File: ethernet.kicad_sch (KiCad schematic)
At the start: 1 part, among them U1 MIMX8MN5DVPIZAA

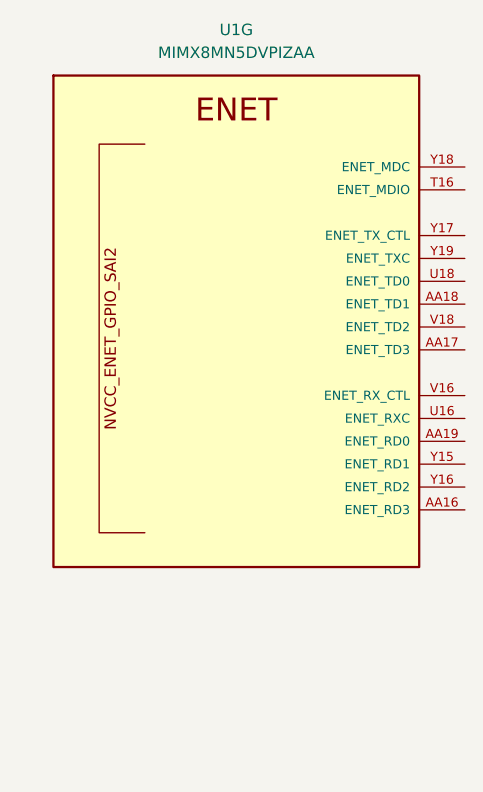
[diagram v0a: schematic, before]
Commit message: move to i.MX8M Mini
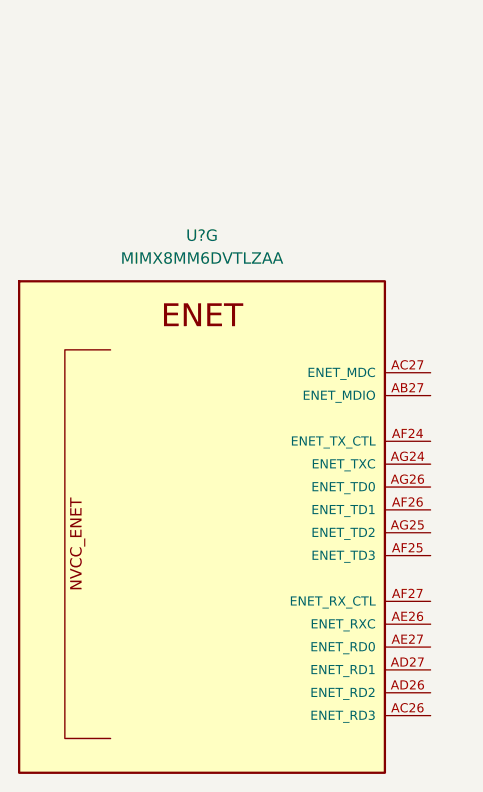
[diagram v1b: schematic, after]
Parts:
- removed U1: MIMX8MN5DVPIZAA, qsbc:SOT1967-1, symbol qsbc:MIMX8MN5DVPIZAA
- added U?: MIMX8MM6DVTLZAA, qsbc:SOT1967-1, symbol qsbc:MIMX8MM6DVTLZAA

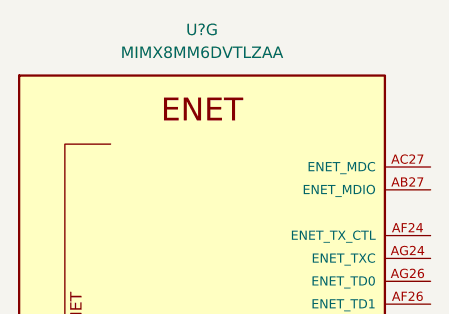
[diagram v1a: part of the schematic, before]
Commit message: ddr sch done
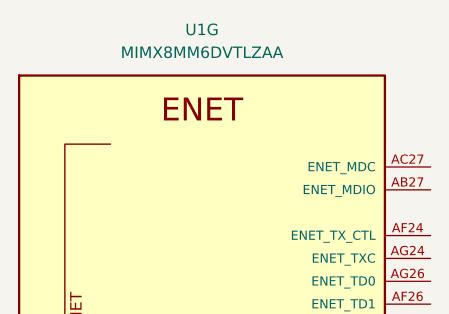
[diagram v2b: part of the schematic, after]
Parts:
- gave numbers to parts that had none: 1
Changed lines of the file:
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@@
   (symbol (lib_id "qsbc:MIMX8MM6DVTLZAA") (at 114.3 90.17 0) (unit 7)
     (in_bom yes) (on_board yes) (fields_autoplaced)
-    (property "Reference" "U?" (id 0) (at 114.3 71.12 0))
+    (property "Reference" "U1" (id 0) (at 114.3 71.12 0))
     (property "Value" "MIMX8MM6DVTLZAA" (id 1) (at 114.3 73.66 0))
     (property "Footprint" "qsbc:SOT1967-1" (id 2) (at 118.11 280.67 0)

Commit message: misc work, usb sch done
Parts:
- added J4: ARJM11D7-502-AB-EW2, qsbc:ARJM11D7-502-AB-EW2, symbol qsbc:ARJM11D7-502-AB-EW2
- added U13, U14: TPD4EUSB30, Package_SON:USON-10_2.5x1.0mm_P0.5mm, symbol qsbc:TPD4EUSB30
- added U18: RTL8211F, Package_DFN_QFN:QFN-40-1EP_5x5mm_P0.4mm_EP3.6x3.6mm_ThermalVias, symbol qsbc:RTL8211F
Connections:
- new net: U14.1 (D1+), U14.10
- new net: U14.2 (D1-), U14.9
- new net: U14.3 (GND), U14.8 (GND)
- new net: U14.4 (D2+), U14.7
- new net: U14.5 (D2-), U14.6
- new net: U13.1 (D1+), U13.10
- new net: U13.2 (D1-), U13.9
- new net: U13.3 (GND), U13.8 (GND)
- new net: U13.4 (D2+), U13.7
- new net: U13.5 (D2-), U13.6
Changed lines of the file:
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@@
 (kicad_sch (version 20211123) (generator eeschema)
-  (paper "A4")
+  (paper "A3")
+  (symbol (lib_id "qsbc:TPD4EUSB30") (at 275.59 53.34 0) (unit 1)
+    (in_bom yes) (on_board yes) (fields_autoplaced)
+    (property "Reference" "U14" (id 0) (at 275.59 40.64 0))
+    (property "Value" "TPD4EUSB30" (id 1) (at 275.59 43.18 0))
+    (property "Footprint" "Package_SON:USON-10_2.5x1.0mm_P0.5mm" (id 2) (at 251.46 63.5 0)
+      (effects (font (size 1.27 1.27)) hide)
+    )
+    (property "Datasheet" "http://www.ti.com/lit/ds/symlink/tpd2eusb30a.pdf" (id 3) (at 275.59 53.34 0)
+      (effects (font (size 1.27 1.27)) hide)
+    )
+    (pin "1")
+    (pin "10")
+    (pin "2")
+    (pin "3")
+    (pin "4")
+    (pin "5")
+    (pin "6")
+    (pin "7")
+    (pin "8")
+    (pin "9")
+  )
+  (symbol (lib_id "qsbc:ARJM11D7-502-AB-EW2") (at 318.77 130.81 0) (unit 1)
+    (in_bom yes) (on_board yes) (fields_autoplaced)
+    (property "Reference" "J4" (id 0) (at 350.52 92.7099 0)
+      (effects (font (size 1.27 1.27)) (justify left))
+    )
+    (property "Value" "ARJM11D7-502-AB-EW2" (id 1) (at 350.52 95.2499 0)
+      (effects (font (size 1.27 1.27)) (justify left))
+    )
+    (property "Footprint" "qsbc:ARJM11D7-502-AB-EW2" (id 2) (at 336.55 140.97 0)
+      (effects (font (size 1.27 1.27)) hide)
+    )
+    (property "Datasheet" "https://abracon.com/Magnetics/ARJM11.pdf" (id 3) (at 340.36 138.43 0)
+      (effects (font (size 1.27 1.27)) hide)
+    )
+    (pin "1")
+    (pin "10")
+    (pin "11")
+    (pin "12")
+    (pin "13")
+    (pin "14")
+    (pin "15")
+    (pin "16")
+    (pin "2")
+    (pin "3")
+    (pin "4")
+    (pin "5")
+    (pin "6")
+    (pin "7")
+    (pin "8")
+    (pin "9")
+  )
   (symbol (lib_id "qsbc:MIMX8MM6DVTLZAA") (at 114.3 90.17 0) (unit 7)
     (in_bom yes) (on_board yes) (fields_autoplaced)
@@
     (pin "D19")
   )
+  (symbol (lib_id "qsbc:TPD4EUSB30") (at 273.05 96.52 0) (unit 1)
+    (in_bom yes) (on_board yes) (fields_autoplaced)
+    (property "Reference" "U13" (id 0) (at 273.05 83.82 0))
+    (property "Value" "TPD4EUSB30" (id 1) (at 273.05 86.36 0))
+    (property "Footprint" "Package_SON:USON-10_2.5x1.0mm_P0.5mm" (id 2) (at 248.92 106.68 0)
+      (effects (font (size 1.27 1.27)) hide)
+    )
+    (property "Datasheet" "http://www.ti.com/lit/ds/symlink/tpd2eusb30a.pdf" (id 3) (at 273.05 96.52 0)
+      (effects (font (size 1.27 1.27)) hide)
+    )
+    (pin "1")
+    (pin "10")
+    (pin "2")
+    (pin "3")
+    (pin "4")
+    (pin "5")
+    (pin "6")
+    (pin "7")
+    (pin "8")
+    (pin "9")
+  )
+  (symbol (lib_id "qsbc:RTL8211F") (at 217.17 158.75 0) (unit 1)
+    (in_bom yes) (on_board yes) (fields_autoplaced)
+    (property "Reference" "U18" (id 0) (at 217.17 148.59 0))
+    (property "Value" "RTL8211F" (id 1) (at 217.17 151.13 0))
+    (property "Footprint" "Package_DFN_QFN:QFN-40-1EP_5x5mm_P0.4mm_EP3.6x3.6mm_ThermalVias" (id 2) (at 260.35 241.3 0)
+      (effects (font (size 1.27 1.27)) hide)
+    )
+    (property "Datasheet" "https://datasheet.lcsc.com/lcsc/1912111437_Realtek-Semicon-RTL8211F-CG_C187932.pdf" (id 3) (at 267.97 245.11 0)
+      (effects (font (size 1.27 1.27)) hide)
+    )
+    (pin "11")
+    (pin "12")
+    (pin "13")
+    (pin "14")
+    (pin "15")
+    (pin "16")
+    (pin "17")
+    (pin "18")
+    (pin "19")
+    (pin "20")
+    (pin "21")
+    (pin "22")
+    (pin "23")
+    (pin "24")
+    (pin "25")
+    (pin "26")
+    (pin "27")
+    (pin "28")
+    (pin "29")
+    (pin "3")
+    (pin "30")
+    (pin "31")
+    (pin "32")
+    (pin "33")
+    (pin "34")
+    (pin "35")
+    (pin "36")
+    (pin "37")
+    (pin "38")
+    (pin "39")
+    (pin "40")
+    (pin "41")
+    (pin "8")
+    (pin "1")
+    (pin "10")
+    (pin "2")
+    (pin "4")
+    (pin "5")
+    (pin "6")
+    (pin "7")
+    (pin "9")
+  )
 )

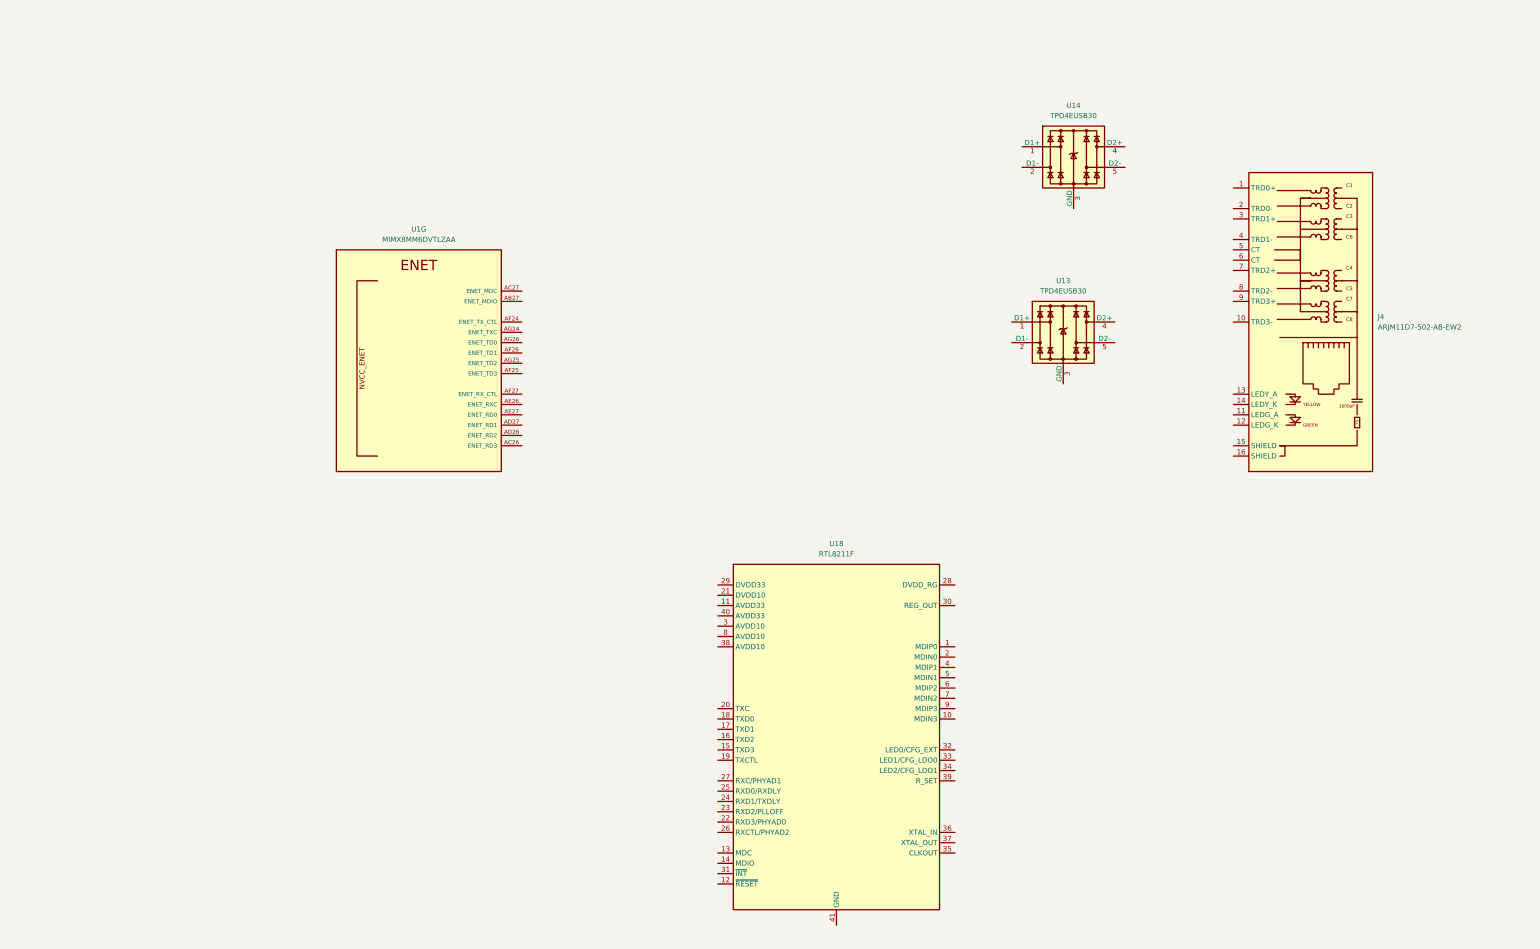
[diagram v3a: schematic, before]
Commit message: enet sch done, other misc sch work
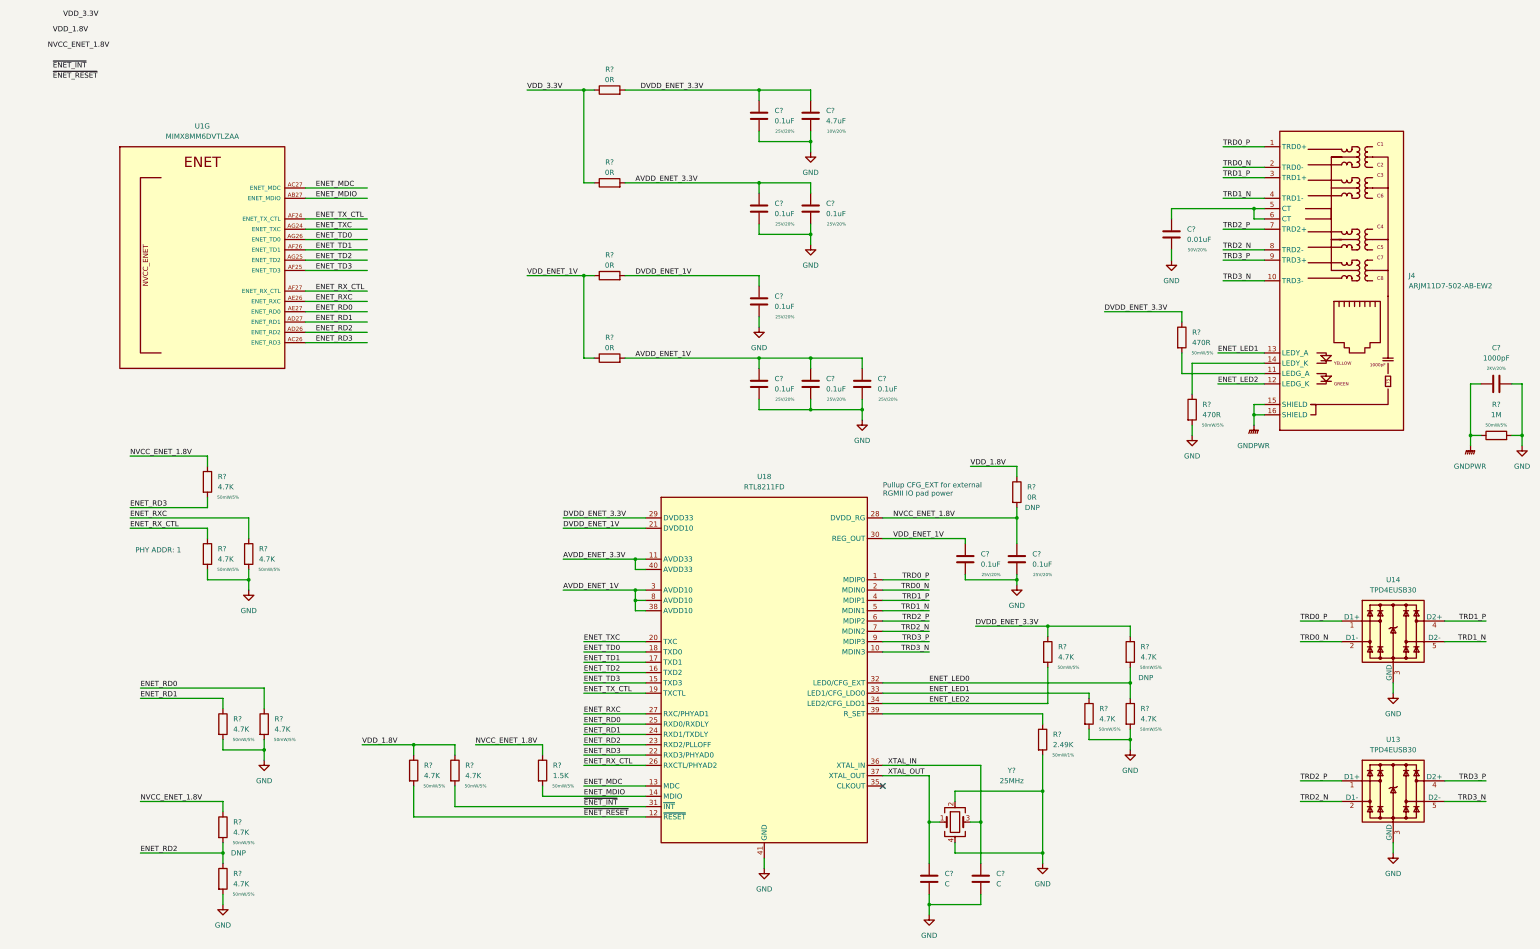
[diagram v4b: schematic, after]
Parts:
- added C? (x9): 0.1uF, Capacitor_SMD:C_0402_1005Metric, symbol Device:C
- added C?: 4.7uF, Capacitor_SMD:C_0402_1005Metric, symbol Device:C
- added C?: 1000pF, Capacitor_SMD:C_1210_3225Metric, symbol Device:C
- added C?: 0.01uF, Capacitor_SMD:C_0603_1608Metric, symbol Device:C
- added C? (x2): C, Capacitor_SMD:C_0402_1005Metric, symbol Device:C
- added R? (x13): 4.7K, Resistor_SMD:R_0402_1005Metric, symbol Device:R
- added R? (x5): 0R, Resistor_SMD:R_0402_1005Metric, symbol Device:R
- added R?: 2.49K, Resistor_SMD:R_0402_1005Metric, symbol Device:R
- added R? (x2): 470R, Resistor_SMD:R_0402_1005Metric, symbol Device:R
- added R?: 1M, Resistor_SMD:R_1206_3216Metric, symbol Device:R
- added R?: 1.5K, Resistor_SMD:R_0402_1005Metric, symbol Device:R
- added Y?: 25MHz, symbol Device:Crystal_GND24
- U18: value RTL8211F -> RTL8211FD
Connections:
- net TRD0_P: now reaches U14.1 (D1+), U14.10
- net TRD0_P: now also J4.1 (TRD0+), U18.1 (MDIP0)
- net TRD0_N: now reaches U14.2 (D1-), U14.9
- net TRD0_N: now also J4.2 (TRD0-), U18.2 (MDIN0)
- net GND: now reaches U14.3 (GND), U14.8 (GND)
- net GND: now also U13.3 (GND), U13.8 (GND), U18.41 (GND), C?.2, C?.2, C?.2, C?.2, C?.2, C?.2, C?.2, C?.2, C?.2, C?.2, C?.2, C?.2, C?.2, C?.2, R?.2, R?.2, R?.2, R?.2, R?.2, R?.2, R?.2, R?.2, R?.2, R?.2, Y?.2, Y?.4
- net TRD1_P: now reaches U14.4 (D2+), U14.7
- net TRD1_P: now also J4.3 (TRD1+), U18.4 (MDIP1)
- net TRD1_N: now reaches U14.5 (D2-), U14.6
- net TRD1_N: now also J4.4 (TRD1-), U18.5 (MDIN1)
- net TRD3_N: now reaches J4.10 (TRD3-)
- net TRD3_N: now also U13.5 (D2-), U13.6, U18.10 (MDIN3)
- net at J4.11 (LEDG_A): now also R?.2
- net ENET_LED2: now reaches J4.12 (LEDG_K)
- net ENET_LED2: now also U18.34 (LED2/CFG_LDO1), R?.2
- net ENET_LED1: now reaches J4.13 (LEDY_A)
- net ENET_LED1: now also U18.33 (LED1/CFG_LDO0), R?.1
- net at J4.14 (LEDY_K): now also R?.1
- net GNDPWR: now reaches J4.15 (SHIELD)
- net GNDPWR: now also J4.16 (SHIELD), C?.1, R?.1
- net at J4.5 (CT): now also J4.6 (CT), C?.1
- net TRD2_P: now reaches J4.7 (TRD2+)
- net TRD2_P: now also U13.1 (D1+), U13.10, U18.6 (MDIP2)
- net TRD2_N: now reaches J4.8 (TRD2-)
- net TRD2_N: now also U13.2 (D1-), U13.9, U18.7 (MDIN2)
- net TRD3_P: now reaches J4.9 (TRD3+)
- net TRD3_P: now also U13.4 (D2+), U13.7, U18.9 (MDIP3)
- net ENET_MDIO: now reaches U1.AB27 (ENET_MDIO)
- net ENET_MDIO: now also U18.14 (MDIO), R?.2
- net ENET_RD3: now reaches U1.AC26 (ENET_RD3)
- net ENET_RD3: now also U18.22 (RXD3/PHYAD0), R?.2
- net ENET_MDC: now reaches U1.AC27 (ENET_MDC)
- net ENET_MDC: now also U18.13 (MDC)
- net ENET_RD2: now reaches U1.AD26 (ENET_RD2)
- net ENET_RD2: now also U18.23 (RXD2/PLLOFF), R?.1, R?.2
- net ENET_RD1: now reaches U1.AD27 (ENET_RD1)
- net ENET_RD1: now also U18.24 (RXD1/TXDLY), R?.1
- net ENET_RXC: now reaches U1.AE26 (ENET_RXC)
- net ENET_RXC: now also U18.27 (RXC/PHYAD1), R?.1
- net ENET_RD0: now reaches U1.AE27 (ENET_RD0)
- net ENET_RD0: now also U18.25 (RXD0/RXDLY), R?.1
- net ENET_TX_CTL: now reaches U1.AF24 (ENET_TX_CTL)
- net ENET_TX_CTL: now also U18.19 (TXCTL)
- net ENET_TD3: now reaches U1.AF25 (ENET_TD3)
- net ENET_TD3: now also U18.15 (TXD3)
- net ENET_TD1: now reaches U1.AF26 (ENET_TD1)
- net ENET_TD1: now also U18.17 (TXD1)
- net ENET_RX_CTL: now reaches U1.AF27 (ENET_RX_CTL)
- net ENET_RX_CTL: now also U18.26 (RXCTL/PHYAD2), R?.1
- net ENET_TXC: now reaches U1.AG24 (ENET_TXC)
- net ENET_TXC: now also U18.20 (TXC)
- net ENET_TD2: now reaches U1.AG25 (ENET_TD2)
- net ENET_TD2: now also U18.16 (TXD2)
- net ENET_TD0: now reaches U1.AG26 (ENET_TD0)
- net ENET_TD0: now also U18.18 (TXD0)
- net AVDD_ENET_3.3V: now reaches U18.11 (AVDD33)
- net AVDD_ENET_3.3V: now also U18.40 (AVDD33), C?.1, C?.1, R?.2
- net ~{ENET_RESET}: now reaches U18.12 (~{RESET})
- net ~{ENET_RESET}: now also R?.2
- net DVDD_ENET_1V: now reaches U18.21 (DVDD10)
- net DVDD_ENET_1V: now also C?.1, R?.2
- net NVCC_ENET_1.8V: now reaches U18.28 (DVDD_RG)
- net NVCC_ENET_1.8V: now also C?.1, R?.1, R?.1, R?.1, R?.2
- net DVDD_ENET_3.3V: now reaches U18.29 (DVDD33)
- net DVDD_ENET_3.3V: now also C?.1, C?.1, R?.1, R?.1, R?.1, R?.2
- net AVDD_ENET_1V: now reaches U18.3 (AVDD10)
- net AVDD_ENET_1V: now also U18.38 (AVDD10), U18.8 (AVDD10), C?.1, C?.1, C?.1, R?.2
- net VDD_ENET_1V: now reaches U18.30 (REG_OUT)
- net VDD_ENET_1V: now also C?.1, R?.1, R?.1
- net ~{ENET_INT}: now reaches U18.31 (~{INT})
- net ~{ENET_INT}: now also R?.2
- net ENET_LED0: now reaches U18.32 (LED0/CFG_EXT)
- net ENET_LED0: now also R?.1, R?.2
- net XTAL_IN: now reaches U18.36 (XTAL_IN)
- net XTAL_IN: now also C?.1, Y?.3
- net XTAL_OUT: now reaches U18.37 (XTAL_OUT)
- net XTAL_OUT: now also C?.1, Y?.1
- net at U18.39 (R_SET): now also R?.1
- new net VDD_1.8V: R?.1, R?.1, R?.1
- new net VDD_3.3V: R?.1, R?.1
- no-connect marks 0 -> 1
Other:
- note added: "PHY ADDR: 1"
- note added: "Pullup CFG_EXT for external RGMII IO pad power"
- moved on the sheet: J4, U13, U14, U18, U1G

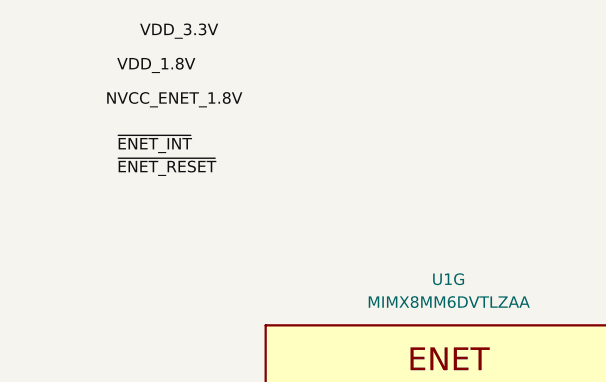
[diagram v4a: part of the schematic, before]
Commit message: enet: add hierarchial labels
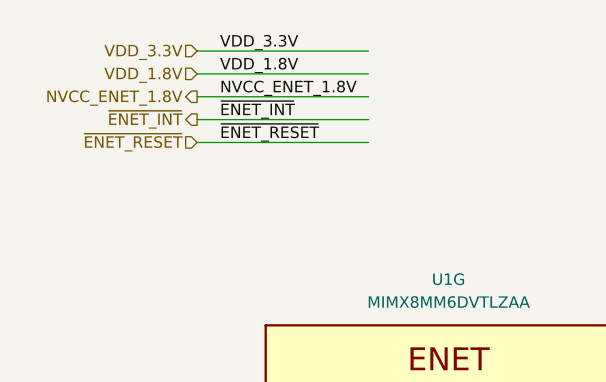
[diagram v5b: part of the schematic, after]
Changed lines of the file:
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@@
+    (stroke (width 0) (type default) (color 0 0 0 0))
+  )
+  (wire (pts (xy 33.02 22.86) (xy 52.07 22.86))
     (stroke (width 0) (type default) (color 0 0 0 0))
   )
@@
     (stroke (width 0) (type default) (color 0 0 0 0))
   )
+  (wire (pts (xy 33.02 27.94) (xy 52.07 27.94))
+    (stroke (width 0) (type default) (color 0 0 0 0))
+  )
   (wire (pts (xy 128.27 198.12) (xy 144.78 198.12))
     (stroke (width 0) (type default) (color 0 0 0 0))
@@
     (stroke (width 0) (type default) (color 0 0 0 0))
   )
+  (wire (pts (xy 33.02 30.48) (xy 52.07 30.48))
+    (stroke (width 0) (type default) (color 0 0 0 0))
+  )
   (wire (pts (xy 228.6 182.88) (xy 289.56 182.88))
     (stroke (width 0) (type default) (color 0 0 0 0))
@@
     (stroke (width 0) (type default) (color 0 0 0 0))
   )
+  (wire (pts (xy 33.02 25.4) (xy 52.07 25.4))
+    (stroke (width 0) (type default) (color 0 0 0 0))
+  )
   (wire (pts (xy 248.92 157.48) (xy 261.62 157.48))
     (stroke (width 0) (type default) (color 0 0 0 0))
@@
     (stroke (width 0) (type default) (color 0 0 0 0))
   )
+  (wire (pts (xy 33.02 20.32) (xy 52.07 20.32))
+    (stroke (width 0) (type default) (color 0 0 0 0))
+  )
   (wire (pts (xy 223.52 113.03) (xy 223.52 115.57))
     (stroke (width 0) (type default) (color 0 0 0 0))
@@
     (effects (font (size 1.27 1.27)) (justify right bottom))
   )
-  (label "~{ENET_INT}" (at 24.13 31.75 0)
+  (label "~{ENET_INT}" (at 35.56 27.94 0)
     (effects (font (size 1.27 1.27)) (justify left bottom))
   )
@@
     (effects (font (size 1.27 1.27)) (justify left bottom))
   )
-  (label "NVCC_ENET_1.8V" (at 22.86 26.67 0)
+  (label "NVCC_ENET_1.8V" (at 35.56 25.4 0)
     (effects (font (size 1.27 1.27)) (justify left bottom))
   )
@@
     (effects (font (size 1.27 1.27)) (justify left bottom))
   )
-  (label "VDD_1.8V" (at 24.13 22.86 0)
+  (label "VDD_1.8V" (at 35.56 22.86 0)
     (effects (font (size 1.27 1.27)) (justify left bottom))
   )
@@
     (effects (font (size 1.27 1.27)) (justify left bottom))
   )
-  (label "VDD_3.3V" (at 26.67 19.05 0)
+  (label "VDD_3.3V" (at 35.56 20.32 0)
     (effects (font (size 1.27 1.27)) (justify left bottom))
   )
@@
     (effects (font (size 1.27 1.27)) (justify left bottom))
   )
-  (label "~{ENET_RESET}" (at 24.13 34.29 0)
+  (label "~{ENET_RESET}" (at 35.56 30.48 0)
     (effects (font (size 1.27 1.27)) (justify left bottom))
   )
@@
     (effects (font (size 1.27 1.27)) (justify left bottom))
   )
+  (hierarchical_label "~{ENET_RESET}" (shape input) (at 33.02 30.48 180)
+    (effects (font (size 1.27 1.27)) (justify right))
+  )
+  (hierarchical_label "~{ENET_INT}" (shape output) (at 33.02 27.94 180)
+    (effects (font (size 1.27 1.27)) (justify right))
+  )
+  (hierarchical_label "NVCC_ENET_1.8V" (shape output) (at 33.02 25.4 180)
+    (effects (font (size 1.27 1.27)) (justify right))
+  )
+  (hierarchical_label "VDD_1.8V" (shape input) (at 33.02 22.86 180)
+    (effects (font (size 1.27 1.27)) (justify right))
+  )
+  (hierarchical_label "VDD_3.3V" (shape input) (at 33.02 20.32 180)
+    (effects (font (size 1.27 1.27)) (justify right))
+  )
   (symbol (lib_id "power:GND") (at 223.52 118.11 0) (unit 1)
